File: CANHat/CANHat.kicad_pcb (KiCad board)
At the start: 2 copper layers, 65 x 56 mm, 21 parts, among them J0 RPi_GPIO, J1 SPI Select, J2 RJ45, J3 RJ45, T1 12V supply, U1 MCP2515, U2 MCP2551, X1 8 MHz

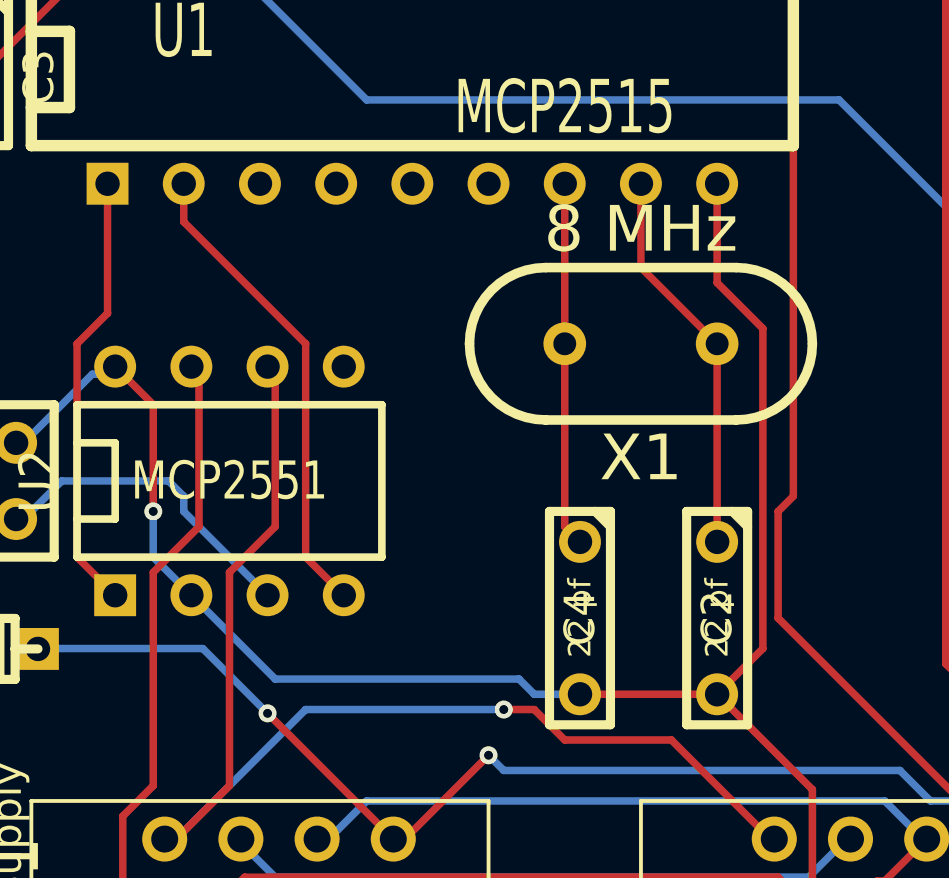
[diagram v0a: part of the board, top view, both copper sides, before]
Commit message: Add level shifting tranceiver => controller (RXD => RXCAN).
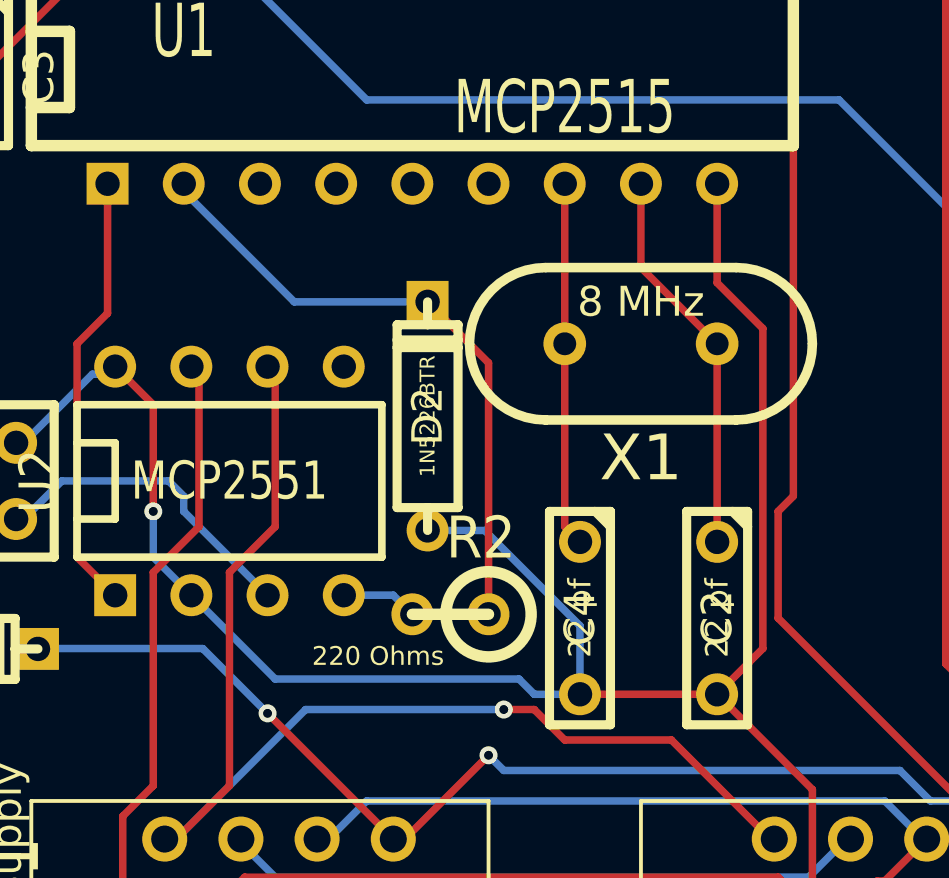
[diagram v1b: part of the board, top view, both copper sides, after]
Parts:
- added D2: 1N5226BTR, D3, F.Cu at (61.0, 59.3)
- added R2: 220 Ohms, R1, F.Cu at (61.7, 65.9)
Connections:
- U1 pad 2: N-0000027 (its old number) -> N-0000011
- U2 pad 4: N-0000027 (its old number) -> N-0000012
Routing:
- net N-0000011: track 0.00 -> 21.2 mm
- net N-0000027 (its old number): track 15.9 -> 0.00 mm
- net GND: track 149.6 -> 158.3 mm
- net N-0000012: track 0.00 -> 2.55 mm

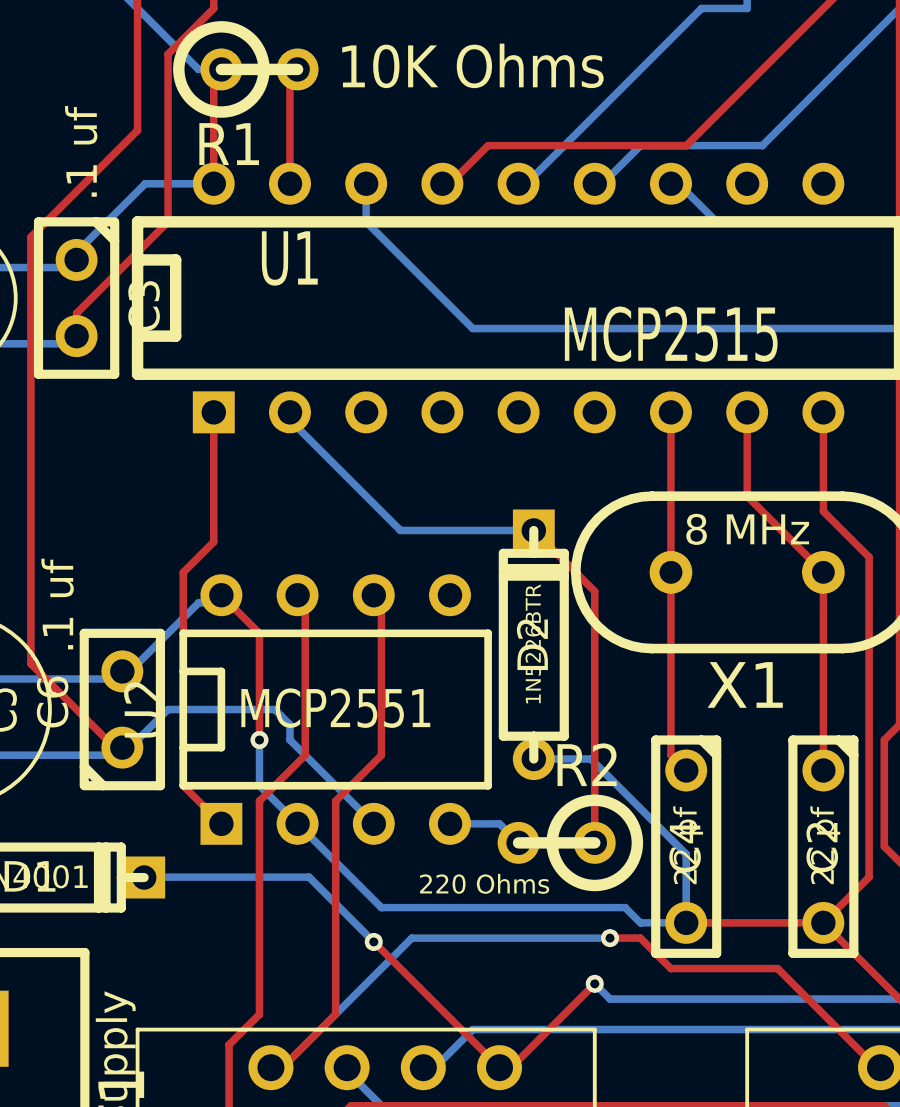
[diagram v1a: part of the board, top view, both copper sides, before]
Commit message: Updates to CAN Hats (incomplete -- waiting on bandwidth)
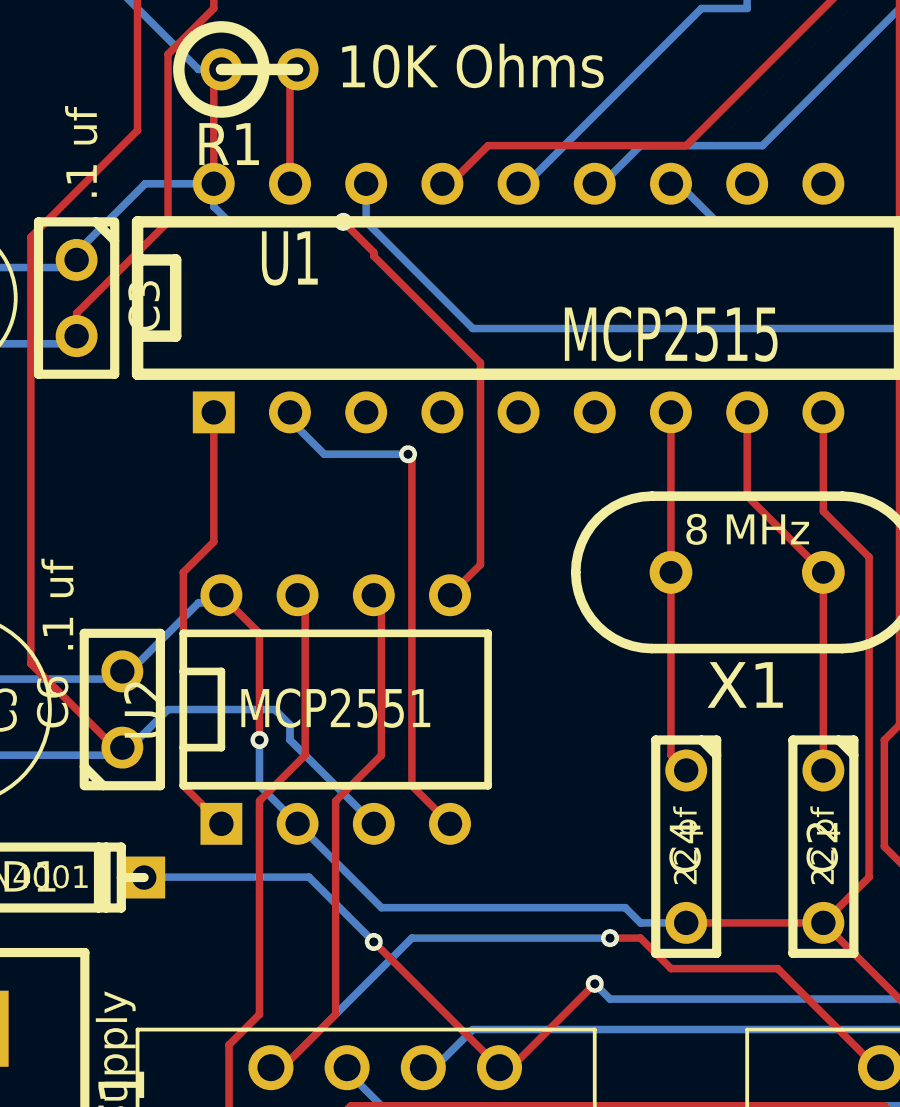
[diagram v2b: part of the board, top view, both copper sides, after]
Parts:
- removed D2: 1N5226BTR, D3
- removed R2: 220 Ohms, R1
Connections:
- U2 pad 4: N-0000012 -> N-0000011
- U2 pad 5: (no net) -> VDD
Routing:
- net VDD: track 21.7 -> 41.7 mm, vias 0 -> 1
- net GND: track 158.3 -> 149.6 mm
- net N-0000011: track 21.2 -> 17.6 mm, vias 0 -> 1
- net N-0000012: track 2.55 -> 0.00 mm

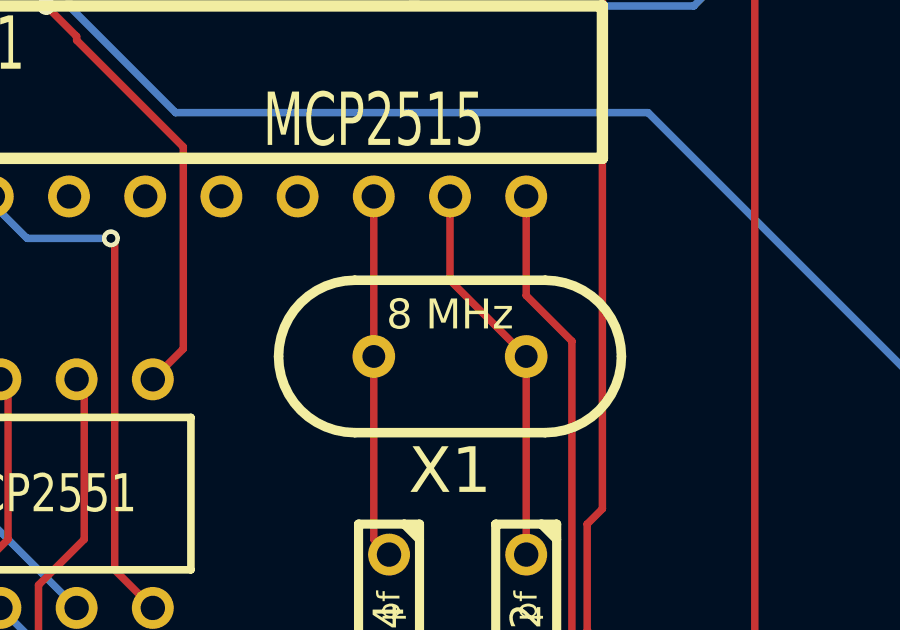
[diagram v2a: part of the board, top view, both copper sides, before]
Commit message: Update to use a 16 mhz cyrstal
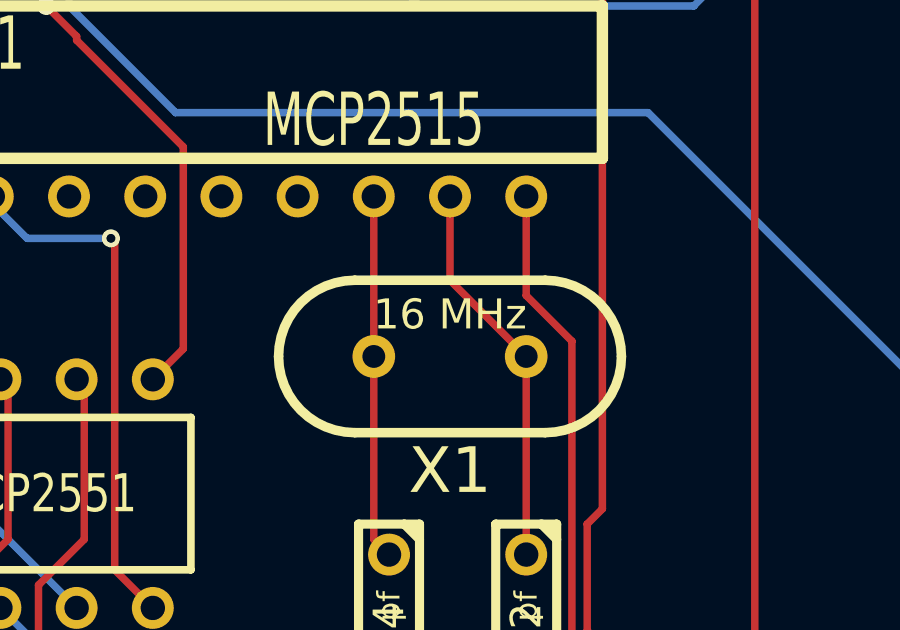
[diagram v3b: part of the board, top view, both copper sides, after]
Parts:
- X1: value 8 MHz -> 16 MHz
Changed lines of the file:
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@@
       (effects (font (size 1.524 1.524) (thickness 0.3048)))
     )
-    (fp_text value "8 MHz" (at 0 1.397 180) (layer F.SilkS)
+    (fp_text value "16 MHz" (at 0 1.397 180) (layer F.SilkS)
       (effects (font (size 1 1) (thickness 0.15)))
     )
@@
   (segment (start 40.386 70.358) (end 40.386 67.056) (width 0.25) (layer F.Cu) (net 2) (status 80000))
   (segment (start 40.386 67.056) (end 40.3528 67.0681) (width 0.25) (layer F.Cu) (net 2) (status 80000))
-  (segment (start 52.832 51.562) (end 52.832 51.816) (width 0.25) (layer B.Cu) (net 3) (status C00000))
-  (segment (start 56.896 64.008) (end 58.166 65.278) (width 0.25) (layer F.Cu) (net 3) (status 800000))
+  (segment (start 52.832 51.562) (end 52.832 51.816) (width 0.25) (layer B.Cu) (net 3))
+  (segment (start 56.896 64.008) (end 58.166 65.278) (width 0.25) (layer F.Cu) (net 3))
   (segment (start 56.896 53.086) (end 56.896 64.008) (width 0.25) (layer F.Cu) (net 3))
   (segment (start 56.769 52.959) (end 56.896 53.086) (width 0.25) (layer F.Cu) (net 3))
   (via (at 56.769 52.959) (size 0.6) (layers F.Cu B.Cu) (net 3))
   (segment (start 53.975 52.959) (end 56.769 52.959) (width 0.25) (layer B.Cu) (net 3))
-  (segment (start 52.832 51.816) (end 53.975 52.959) (width 0.25) (layer B.Cu) (net 3) (status 400000))
+  (segment (start 52.832 51.816) (end 53.975 52.959) (width 0.25) (layer B.Cu) (net 3))
   (segment (start 60.452 43.942) (end 60.452 44.196) (width 0.25) (layer B.Cu) (net 4) (status 80000))
   (segment (start 60.452 44.196) (end 66.548 38.1) (width 0.25) (layer B.Cu) (net 4) (status 80000))
@@
   (segment (start 52.832 61.976) (end 52.832 62.484) (width 0.25) (layer B.Cu) (net 21) (status 80000))
   (segment (start 52.832 62.484) (end 55.626 65.278) (width 0.25) (layer B.Cu) (net 21) (status 80000))
-  (segment (start 50.292 43.942) (end 50.292 44.704) (width 0.25) (layer B.Cu) (net 22) (status 400000))
-  (segment (start 59.182 56.642) (end 58.166 57.658) (width 0.25) (layer F.Cu) (net 22) (status 800000))
+  (segment (start 50.292 43.942) (end 50.292 44.704) (width 0.25) (layer B.Cu) (net 22))
+  (segment (start 59.182 56.642) (end 58.166 57.658) (width 0.25) (layer F.Cu) (net 22))
   (segment (start 59.182 49.911) (end 59.182 56.642) (width 0.25) (layer F.Cu) (net 22))
   (segment (start 55.626 46.355) (end 59.182 49.911) (width 0.25) (layer F.Cu) (net 22))

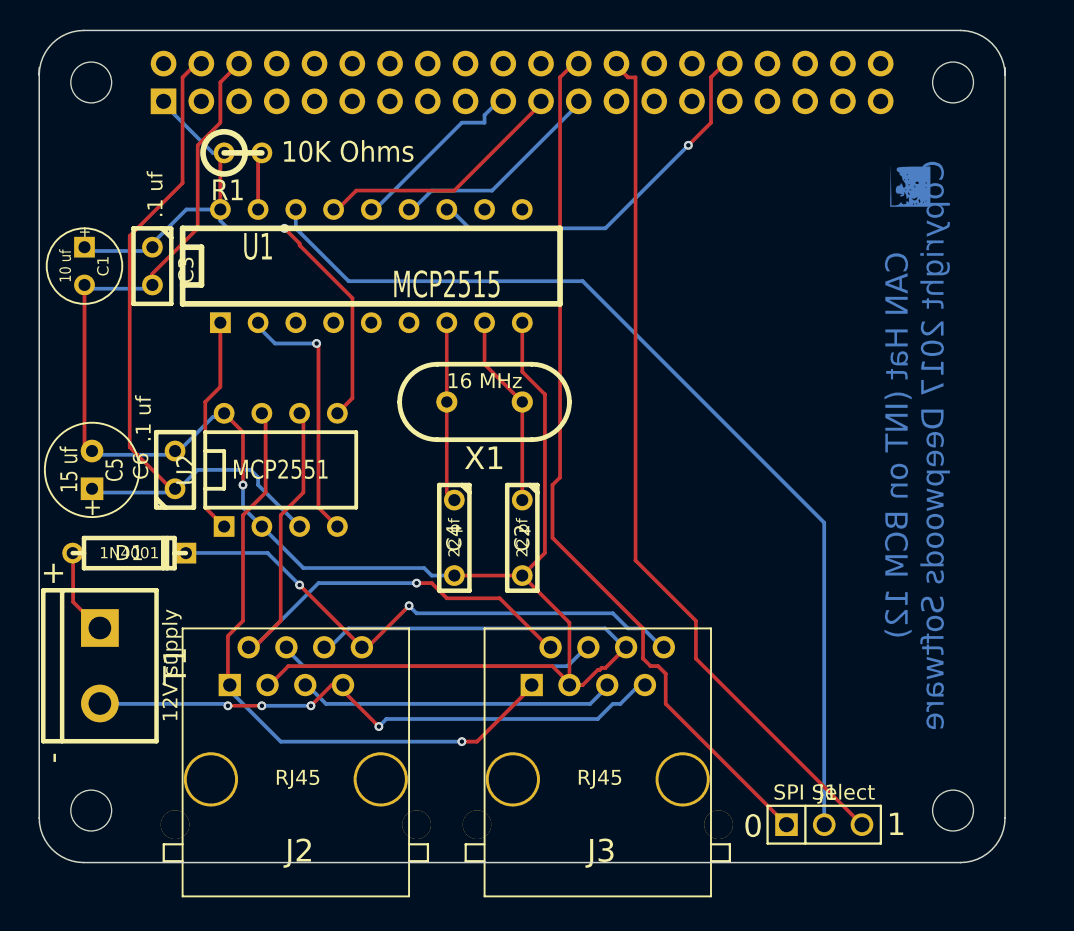
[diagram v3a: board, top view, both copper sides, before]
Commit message: Update (original) CANHat to include powering the tranciever from the LCC and to add on-board termination.
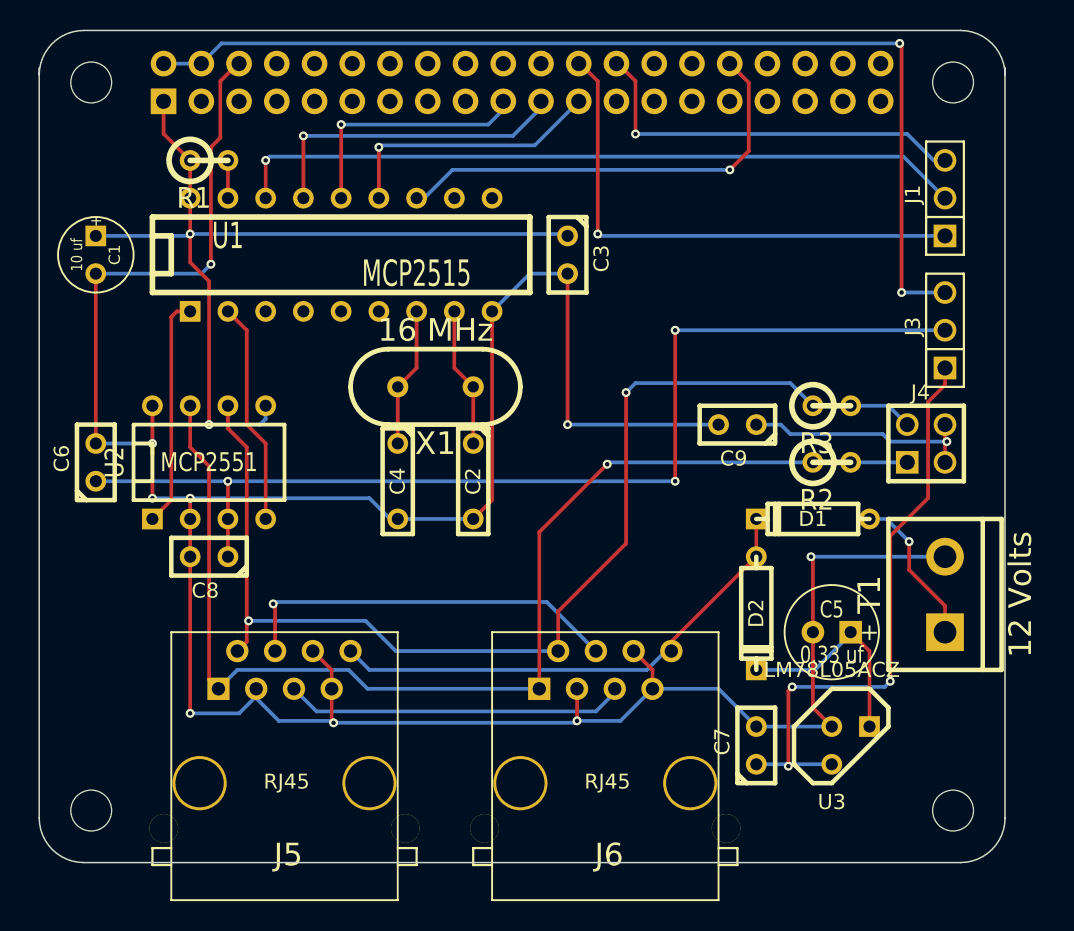
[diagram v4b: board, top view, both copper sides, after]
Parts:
- removed ?: , DWSLogoBCU
- removed J2: RJ45, RJ45_8
- added C7: .1 uf, C1, F.Cu at (86.4, 80.0)
- added C8: .1 uf, C1, F.Cu at (49.5, 67.3)
- added C9: 47 nf, C1, F.Cu at (85.1, 58.4)
- added D2: DIODESCH, D3, F.Cu at (86.4, 71.1)
- added J4: Termination, PIN_ARRAY_2X2, F.Cu at (97.8, 59.7)
- added J5: RJ45, RJ45_8N-S, F.Cu at (54.6, 82.5)
- added J6: RJ45, RJ45_8N-S, F.Cu at (76.2, 82.5)
- added R2: 60 Ohms, R1, F.Cu at (91.4, 61.0)
- added R3: 60 Ohms, R1, F.Cu at (91.4, 57.1)
- added U3: LM78L05ACZ, TO92, F.Cu at (92.7, 80.0)
- C5: value 15 uf -> 0.33 uf
- C6: value .1 uf -> 15 uf
- D1: value 1N4001 -> DIODESCH
- J3: value RJ45 -> PWR Select; footprint RJ45_8 -> PIN_ARRAY_3X1
- T1: value 12V supply -> 12 Volts
- moved T1 57.1 mm to (99.1, 69.8), turned to 90 degrees
- moved C5 51.0 mm to (91.4, 72.4), turned to 180 degrees
- moved D1 46.1 mm to (90.2, 64.8), turned to 180 degrees
- moved J1 42.9 mm to (99.1, 43.2), turned to 90 degrees
- moved J3 38.2 mm to (99.1, 52.1), turned to 90 degrees
- moved C3 28.0 mm to (73.7, 47.0)
- moved C4 5.39 mm to (62.2, 62.2)
- moved C6 5.36 mm to (41.9, 61.0)
- moved C2 5.04 mm to (67.3, 62.2)
- moved U2 4.85 mm to (49.5, 61.0)
- moved X1 3.45 mm to (64.8, 55.9)
- moved R1 2.34 mm to (49.5, 40.6)
- moved U1 2.17 mm to (58.4, 47.0)
- moved C1 1.08 mm to (41.9, 47.0)
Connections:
- C5 pad 1: VCC -> N-0000020
- C6 pad 1: VCC -> +5V
- D1 pad 2: N-000009 (its old number) -> N-000003
- J0 pad 2: (no net) -> +5V (Pi)
- J0 pad 4: VCC -> +5V (Pi)
- J3 pad 1: N-0000015 -> +5V (CAN)
- J3 pad 2: N-0000016 (its old number) -> +5V
- J3 pad 3: GND -> +5V (Pi)
- T1 pad 2: N-000008 (its old number) -> GND
- U2 pad 3: VCC -> +5V
- U2 pad 6: N-0000016 (its old number) -> N-0000014
- U2 pad 7: N-0000015 -> N-0000013
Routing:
- net N-0000013: track 0.00 -> 73.4 mm, vias 0 -> 1
- net +5V: track 0.00 -> 72.4 mm, vias 0 -> 3
- net N-0000014: track 0.00 -> 71.9 mm, vias 0 -> 2
- net +5V (Pi): track 0.00 -> 69.8 mm, vias 0 -> 2
- net GND: track 149.6 -> 201.3 mm, vias 1 -> 9
- net VCC: track 49.9 -> 0.00 mm
- net N-0000016 (its old number): track 42.5 -> 0.00 mm, vias 1 -> 0
- net N-000008 (its old number): track 40.0 -> 0.00 mm, vias 4 -> 0
- net +5V (CAN): track 0.00 -> 40.0 mm, vias 0 -> 3
- net N-000009 (its old number): track 37.9 -> 0.00 mm, vias 2 -> 0
- net N-000003: track 0.00 -> 33.9 mm
- net N-0000010: track 58.8 -> 26.9 mm, vias 0 -> 1
- net N-0000015: track 43.8 -> 16.0 mm
- net N-000005: track 0.00 -> 26.4 mm, vias 0 -> 1
- net N-000009: track 59.0 -> 35.5 mm, vias 0 -> 1
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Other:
- board text removed: "+"
- board text removed: "-"
- board text removed: "0"
- board text removed: "1"
- board text removed: "CAN Hat (INT on BCM 12) Copyright 2017 Deepwoods Software"
